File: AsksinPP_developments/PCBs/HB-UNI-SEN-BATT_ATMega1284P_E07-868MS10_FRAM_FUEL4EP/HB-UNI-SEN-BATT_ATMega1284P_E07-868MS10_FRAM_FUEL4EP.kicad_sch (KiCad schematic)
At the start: 64 parts, among them J1 Conn_01x02, J10 charge, J11 ePaper connector, J12 FTDI Debuger, J13 BME680, J2 Conn_01x02, J3 Conn_01x02, J4 Conn_01x02, J5 ISP Programmer, J6 SHT85, J7 AHT25, J8 AHT20+BMP280, J9 BME280/BMP280, Q1 IRLU024N, SW1 Config button, SW2 Reset button, U1 ATmega1284P-AU, U2 TPS61221DCK, U3 MB85RS2MTPF, U4 MB85RS2MTPF, Y1 8MHz

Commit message: PCBs: KiCAD6 required improvements of layout data bases; added E07-900M10S into FUEL and footprint library
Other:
- title: HB-UNI-SEN-BATT_ATMega1284P_FUEL4EP -> HB-UNI-SEN-BATT_ATMega1284P_E07-868MS10_FRAM_FUEL4EP
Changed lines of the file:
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@@
   (paper "A4")
   (title_block
-    (title "HB-UNI-SEN-BATT_ATMega1284P_FUEL4EP")
-    (date "2023-07-16")
-    (rev "1.2")
+    (title "HB-UNI-SEN-BATT_ATMega1284P_E07-868MS10_FRAM_FUEL4EP")
+    (date "2023-07-24")
+    (rev "1.3")
     (company "FUEL4EP")
     (comment 1 "Creative Commons License, non-commercial")

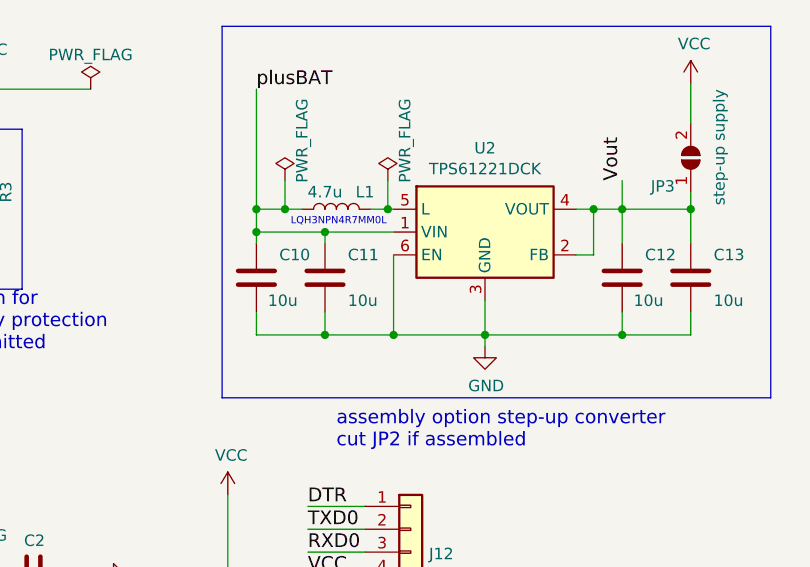
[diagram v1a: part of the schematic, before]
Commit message: HB-UNI-SEN-BATT_ATMega1284P_E07-868MS10_FUEL4EP and HB-UNI-SEN-BATT_ATMega1284P_E07-868MS10_FRAM_FUEL4EP: Fix of wrong connection of EN pin of TPS61221 boost converter
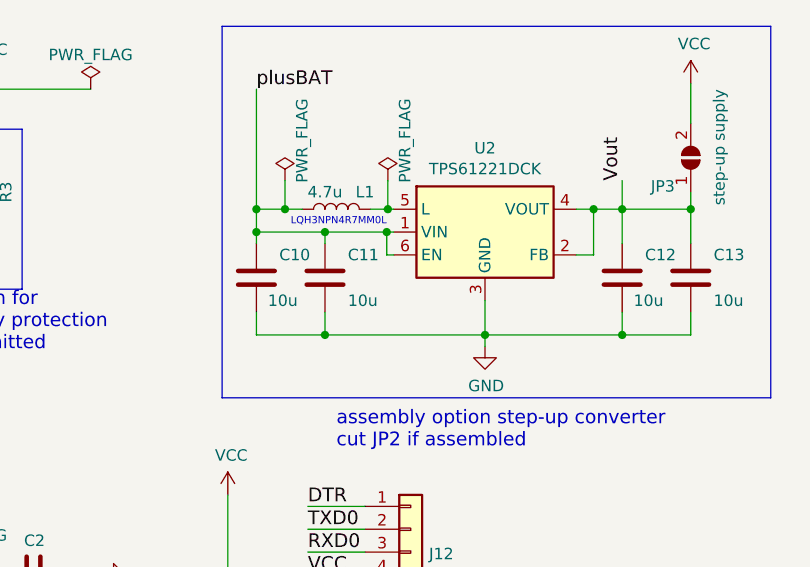
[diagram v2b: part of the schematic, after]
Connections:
- net GND: no longer U2.6 (EN)
- net plusBAT: now also U2.6 (EN)
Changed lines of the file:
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@@
   (title_block
     (title "HB-UNI-SEN-BATT_ATMega1284P_E07-868MS10_FRAM_FUEL4EP")
-    (date "2023-07-24")
-    (rev "1.3")
+    (date "2023-08-15")
+    (rev "1.4")
     (company "FUEL4EP")
     (comment 1 "Creative Commons License, non-commercial")
@@
   (junction (at 77.47 64.135) (diameter 0) (color 0 0 0 0)
   )
-  (junction (at 142.24 49.53) (diameter 0) (color 0 0 0 0)
-  )
   (junction (at 128.905 165.735) (diameter 0) (color 0 0 0 0)
   )
@@
   )
   (junction (at 21.59 33.655) (diameter 0) (color 0 0 0 0)
+  )
+  (junction (at 141.478 38.1) (diameter 0) (color 0 0 0 0)
   )
   (junction (at 134.62 49.53) (diameter 0) (color 0 0 0 0)
@@
     (stroke (width 0) (type default) (color 0 0 0 0))
   )
+  (wire (pts (xy 141.478 38.1) (xy 134.62 38.1))
+    (stroke (width 0) (type default) (color 0 0 0 0))
+  )
   (wire (pts (xy 64.135 108.585) (xy 64.135 106.045))
     (stroke (width 0) (type default) (color 0 0 0 0))
@@
     (stroke (width 0) (type default) (color 0 0 0 0))
   )
-  (wire (pts (xy 134.62 49.53) (xy 142.24 49.53))
+  (wire (pts (xy 134.62 49.53) (xy 152.4 49.53))
     (stroke (width 0) (type default) (color 0 0 0 0))
   )
@@
     (stroke (width 0) (type default) (color 0 0 0 0))
   )
+  (wire (pts (xy 142.24 40.64) (xy 141.478 40.64))
+    (stroke (width 0) (type default) (color 0 0 0 0))
+  )
   (polyline (pts (xy 93.98 35.56) (xy 93.98 26.67))
     (stroke (width 0) (type default) (color 0 0 0 0))
   )
+  (wire (pts (xy 141.478 40.64) (xy 141.478 38.1))
+    (stroke (width 0) (type default) (color 0 0 0 0))
+  )
   (wire (pts (xy 36.195 124.46) (xy 23.495 124.46))
     (stroke (width 0) (type default) (color 0 0 0 0))
@@
     (stroke (width 0) (type default) (color 0 0 0 0))
   )
-  (wire (pts (xy 142.24 40.64) (xy 142.24 49.53))
-    (stroke (width 0) (type default) (color 0 0 0 0))
-  )
   (wire (pts (xy 55.245 47.625) (xy 80.645 47.625))
     (stroke (width 0) (type default) (color 0 0 0 0))
@@
     (stroke (width 0) (type default) (color 0 0 0 0))
   )
-  (wire (pts (xy 142.24 38.1) (xy 134.62 38.1))
+  (wire (pts (xy 142.24 38.1) (xy 141.478 38.1))
     (stroke (width 0) (type default) (color 0 0 0 0))
   )
@@
     (stroke (width 0) (type default) (color 0 0 0 0))
   )
-  (wire (pts (xy 142.24 49.53) (xy 152.4 49.53))
-    (stroke (width 0) (type default) (color 0 0 0 0))
-  )

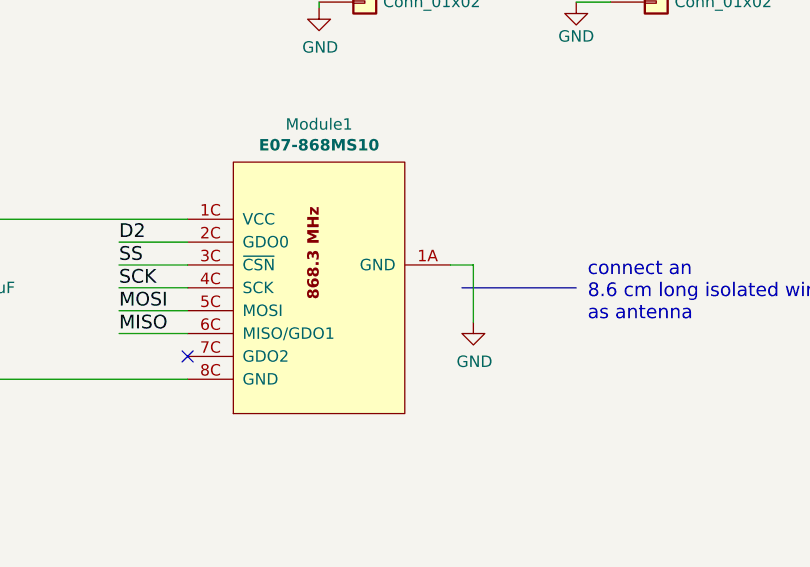
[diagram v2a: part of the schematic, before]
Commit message: PCBs: documentation updates / PCBs: HB-UNI-SEN-BATT_ATMega1284P_E07-868MS10_FUEL4EP, HB-UNI-SEN-BATT_ATMega1284P_E07-868MS10_FRAM_FUEL4EP, HB-UNI-SEN-BATT_ATMega1284P_E07-900MM10S_FUEL4EP: fix of wrong LCSC number for R7
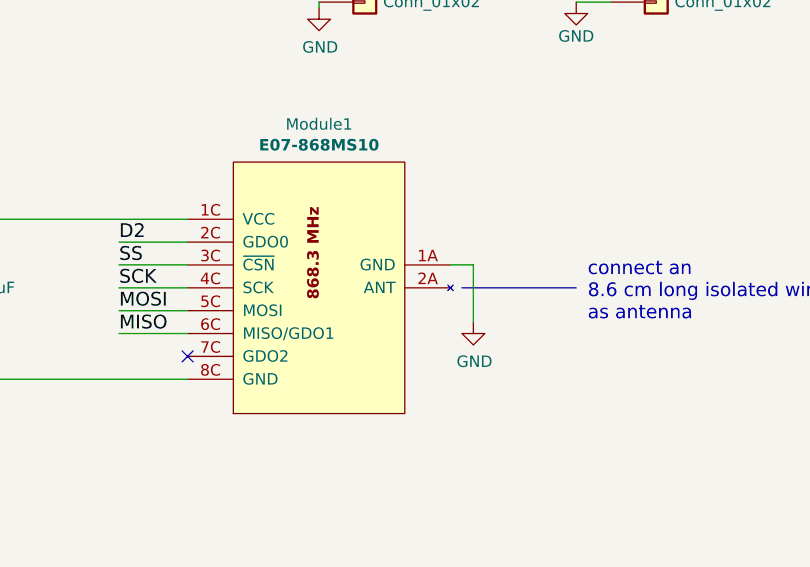
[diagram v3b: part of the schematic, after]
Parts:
- J11: footprint FUEL4EP:PinPads_1x08_P2.00mm_Vertical -> Connector_PinSocket_2.00mm:PinSocket_1x08_P2.00mm_Vertical
- R7: LCSC C340475 -> C149504; TYPE R0805 -> 0805
- U3, U4: footprint FUEL4EP:SOP-8_5.28x5.23mm_P1.27mm -> Package_SO:SOP-8_5.28x5.23mm_P1.27mm

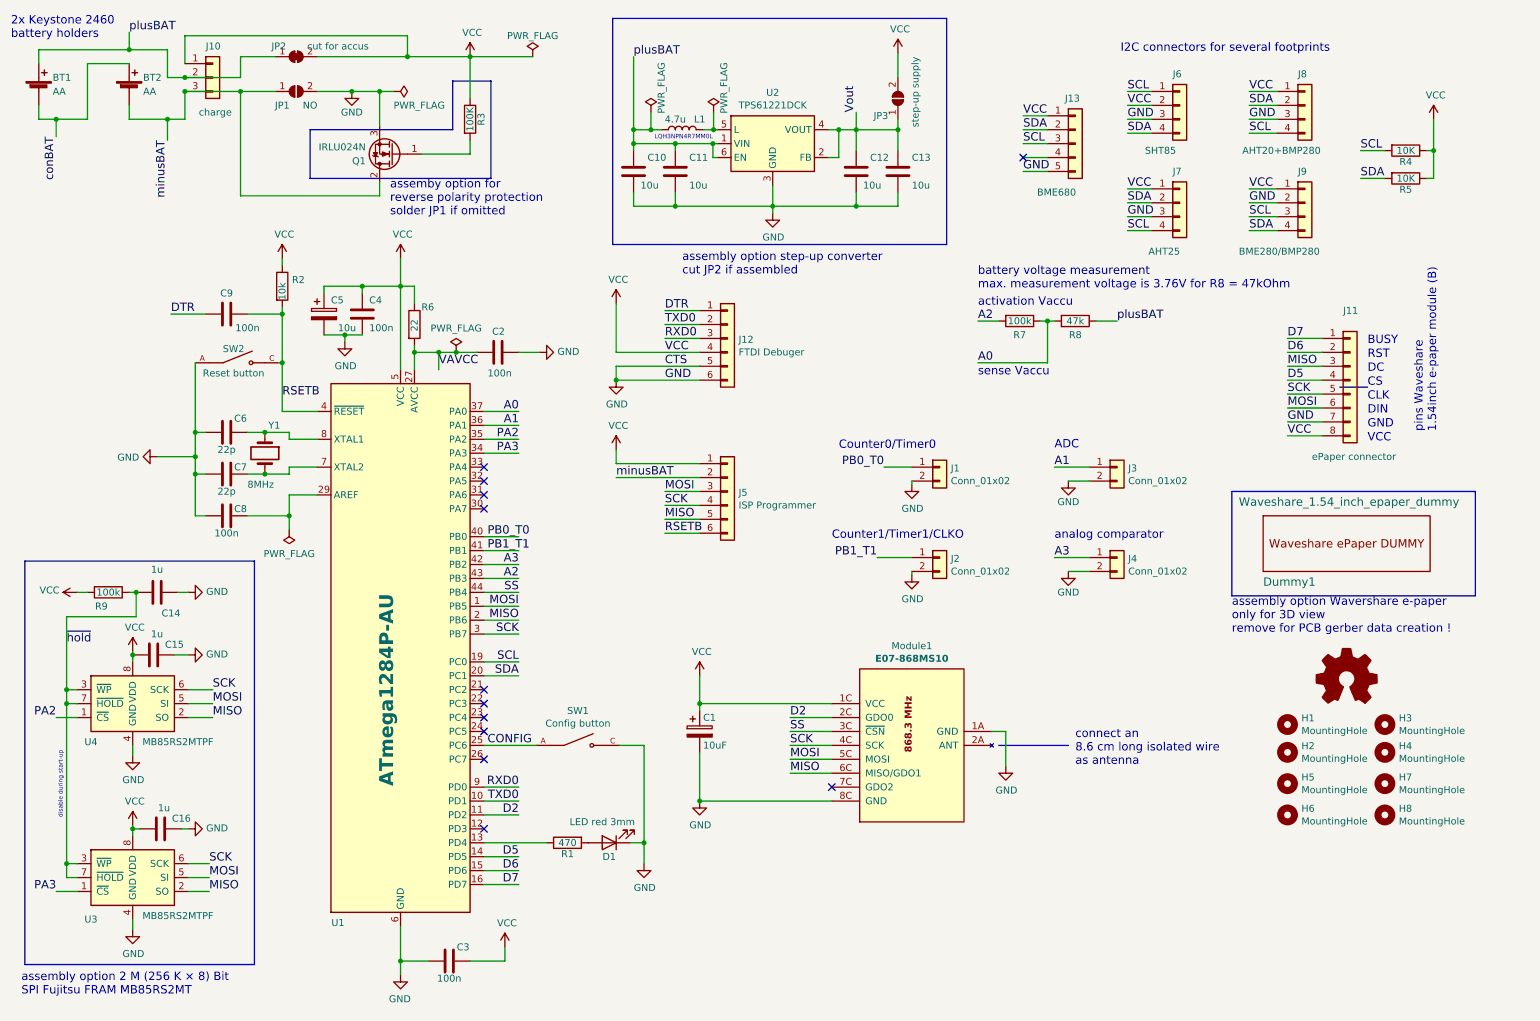
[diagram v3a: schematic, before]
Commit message: PCBs/HB-UNI-SEN-BATT_ATMega1284P_E07-868MS10_FRAM_FUEL4EP: migration to KiCAD 8; fixes of LCSC numbers for JLCPCB assembly
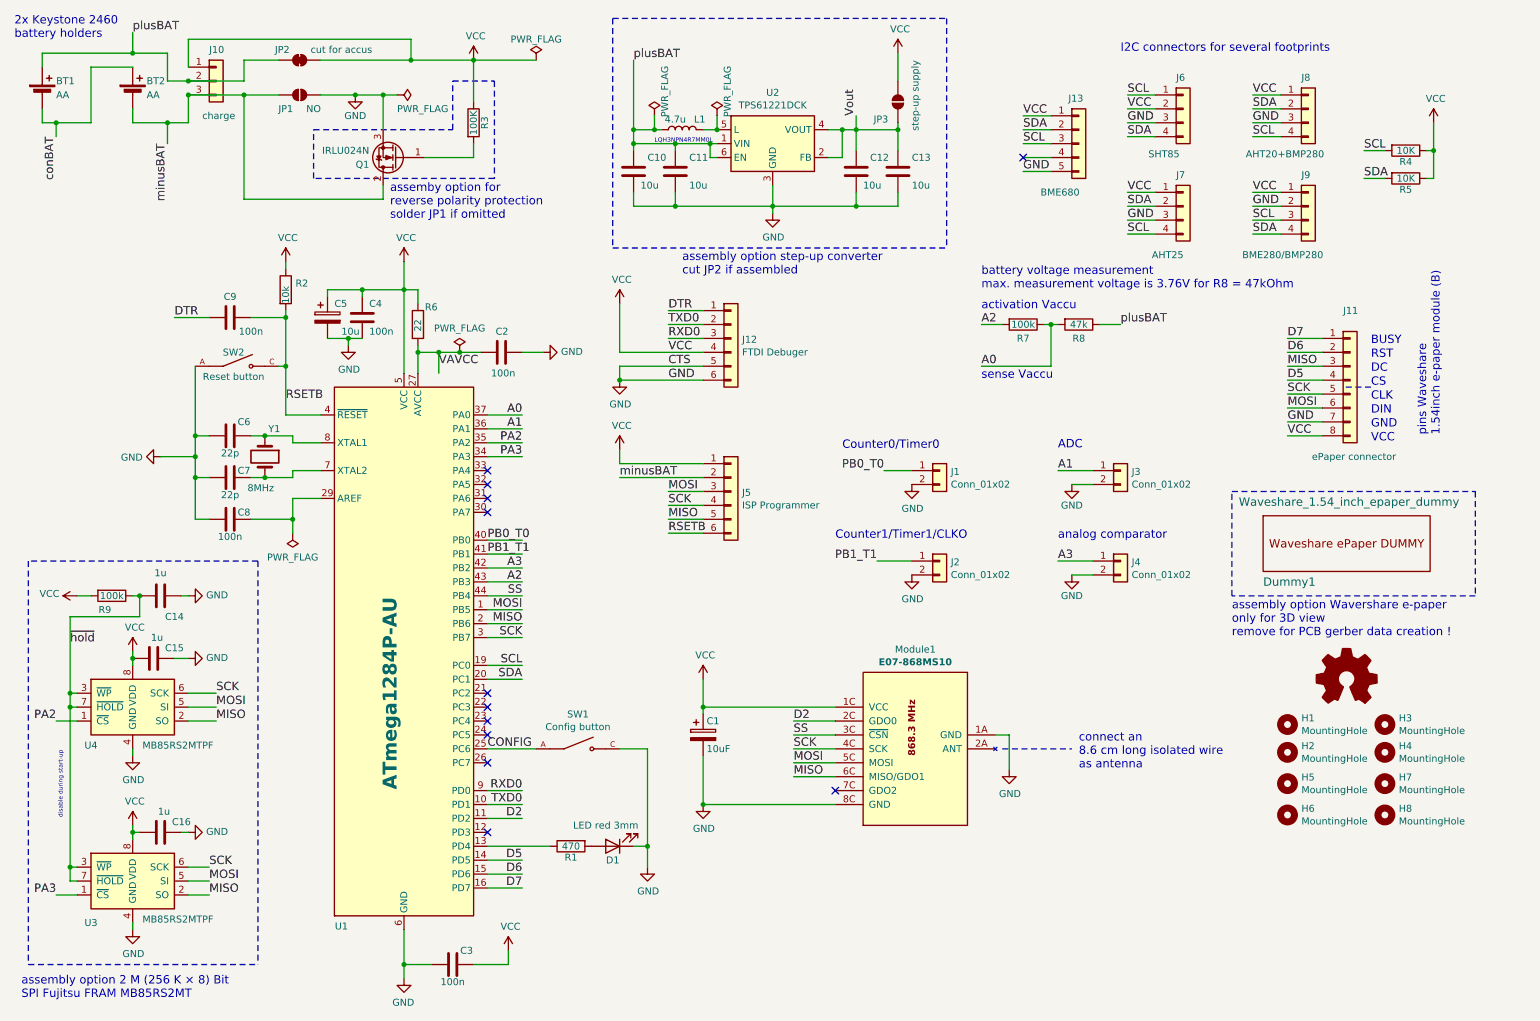
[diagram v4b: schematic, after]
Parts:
- C14, C15, C16: LCSC C15849 -> C28323
- J11: footprint Connector_PinSocket_2.00mm:PinSocket_1x08_P2.00mm_Vertical -> FUEL4EP:PinPads_1x08_P2.00mm_Vertical
- R2: LCSC C101933 -> C17414
- R4, R5: LCSC C101933 -> C17414; TYPE R0805 -> 0805
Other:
- moved on the sheet: BT1, BT2, C1, C14, C15, C16, C2, C3, C4, C5, C6, C7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
